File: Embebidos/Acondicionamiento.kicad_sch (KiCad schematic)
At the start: 23 parts, among them IC1 ESP32-WROVER-B__8MB_, J1 Conn_01x05, J2 Conn_01x08, SW1 SW_Reset, SW2 SW_Boot

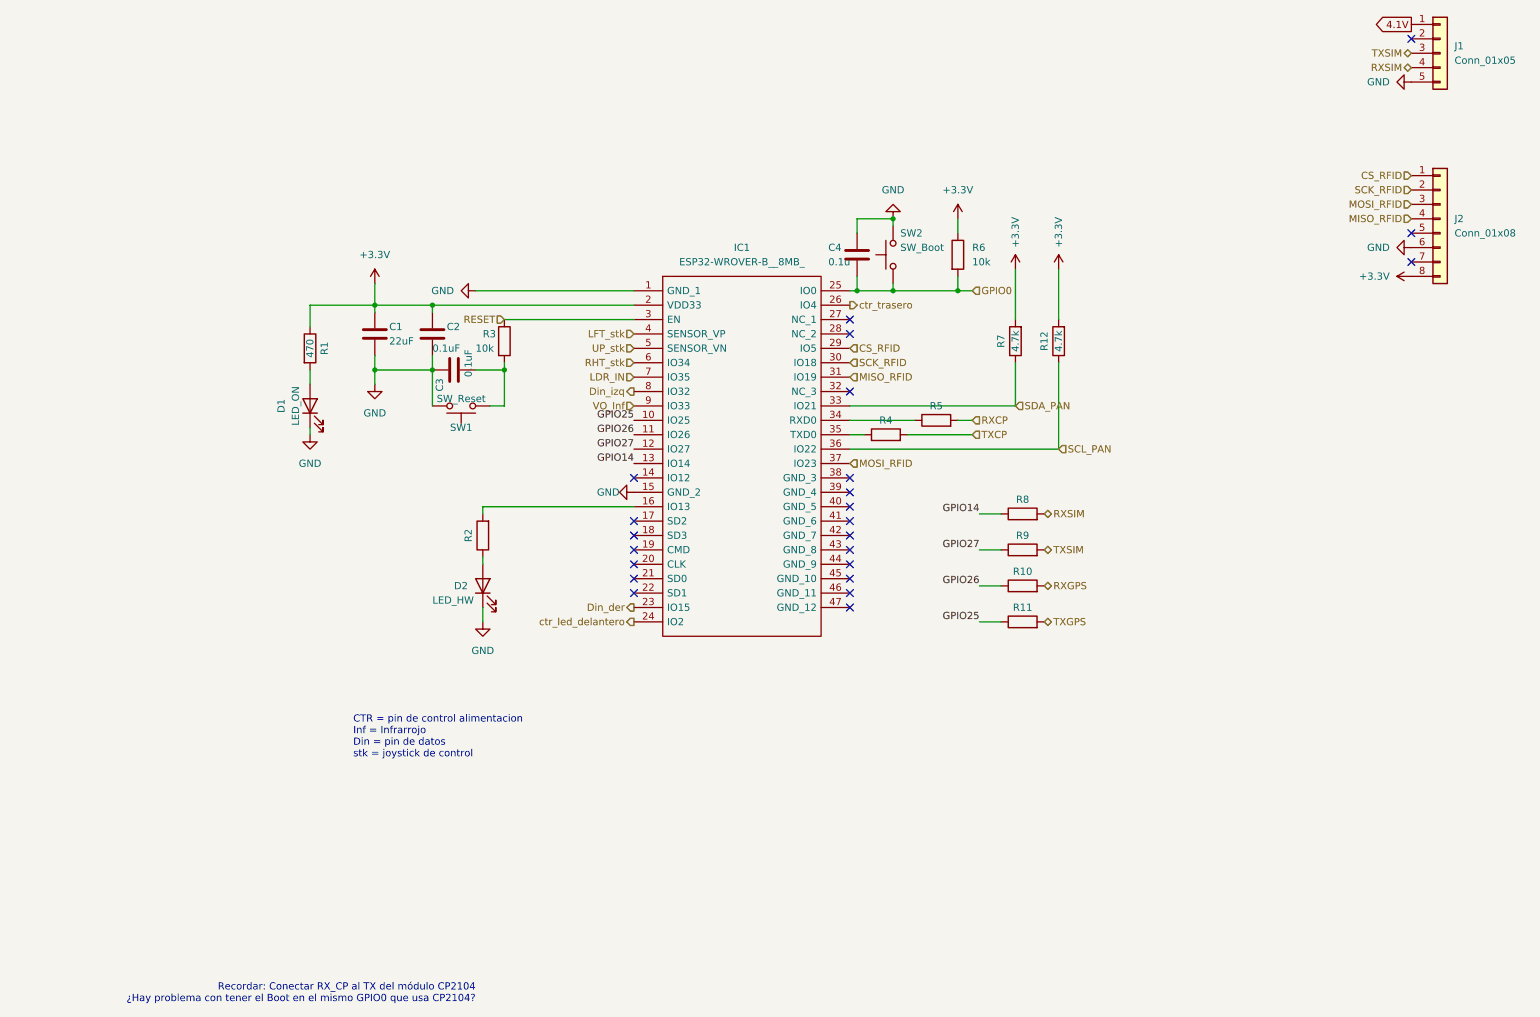
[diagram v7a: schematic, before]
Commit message: Cambios varios
-Conectores movidos a nueva hoja jerarquica

-Transistores DMP colocados en lices delanteras

-Jumpers ubicados para el uso del pin IO13 para SIM800 y LEDHW

-Etiqueta de "no conectado" ubicada en USB_UART
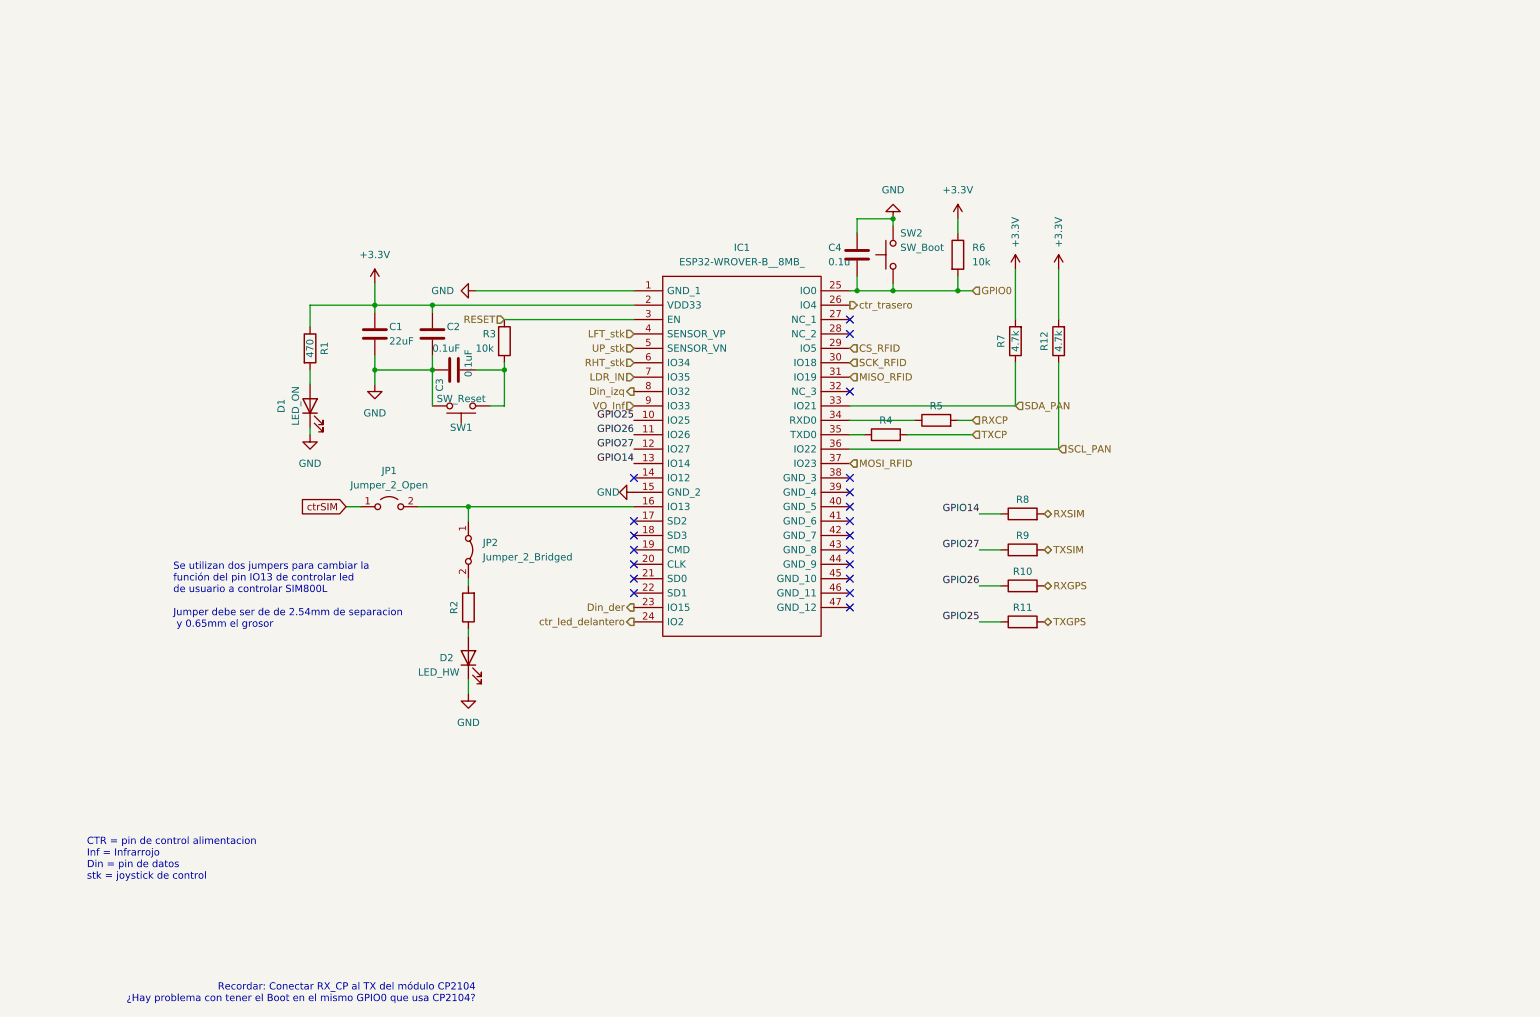
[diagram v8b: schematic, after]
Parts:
- removed J1: Conn_01x05, symbol Connector_Generic:Conn_01x05
- removed J2: Conn_01x08, symbol Connector_Generic:Conn_01x08
- added JP1: Jumper_2_Open, symbol Jumper:Jumper_2_Open
- added JP2: Jumper_2_Bridged, symbol Jumper:Jumper_2_Bridged
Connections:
- net at R2.2: now also JP2.2 (B); no longer IC1.16 (IO13)
- new net: IC1.16 (IO13), JP1.2 (B), JP2.1 (A)
- new net ctrSIM: JP1.1 (A)
- no-connect marks 23 -> 20
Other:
- note added: "Se utilizan dos jumpers para cambiar la función del pin IO13 de controlar led de usuario a controlar SIM800L Jumper debe ser de de 2.54mm de separacion y 0.65mm el grosor"
- moved on the sheet: D2, R2
